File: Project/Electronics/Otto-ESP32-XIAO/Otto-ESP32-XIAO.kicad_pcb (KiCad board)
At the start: 2 copper layers, 60 x 50 mm, 28 parts, among them J1 Conn_01x03, J10 Conn_01x02, J11 Conn_01x04, J12 Conn_01x04, J2 Conn_01x03, J3 Conn_01x03, J4 Conn_01x03, J5 Conn_01x03, J6 Conn_01x03, J7 Conn_01x04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

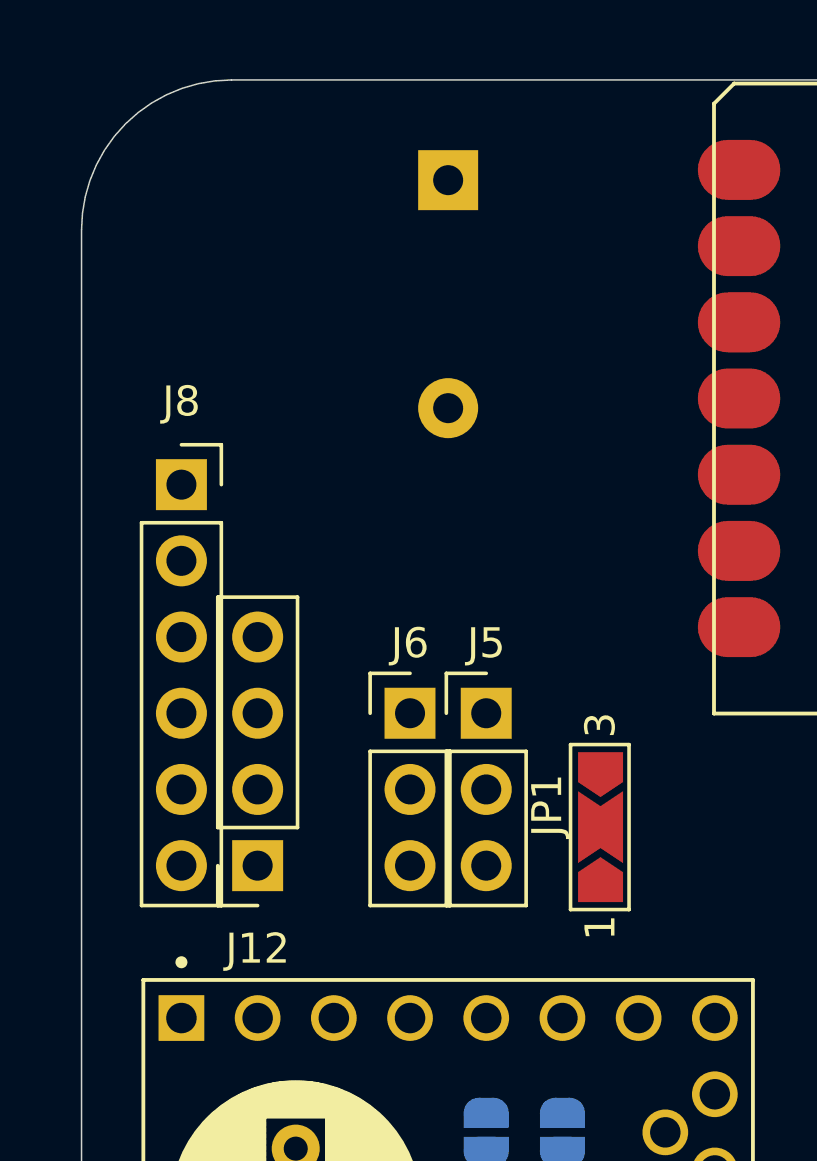
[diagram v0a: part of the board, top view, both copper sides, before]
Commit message: add TMC, oled and 3D models
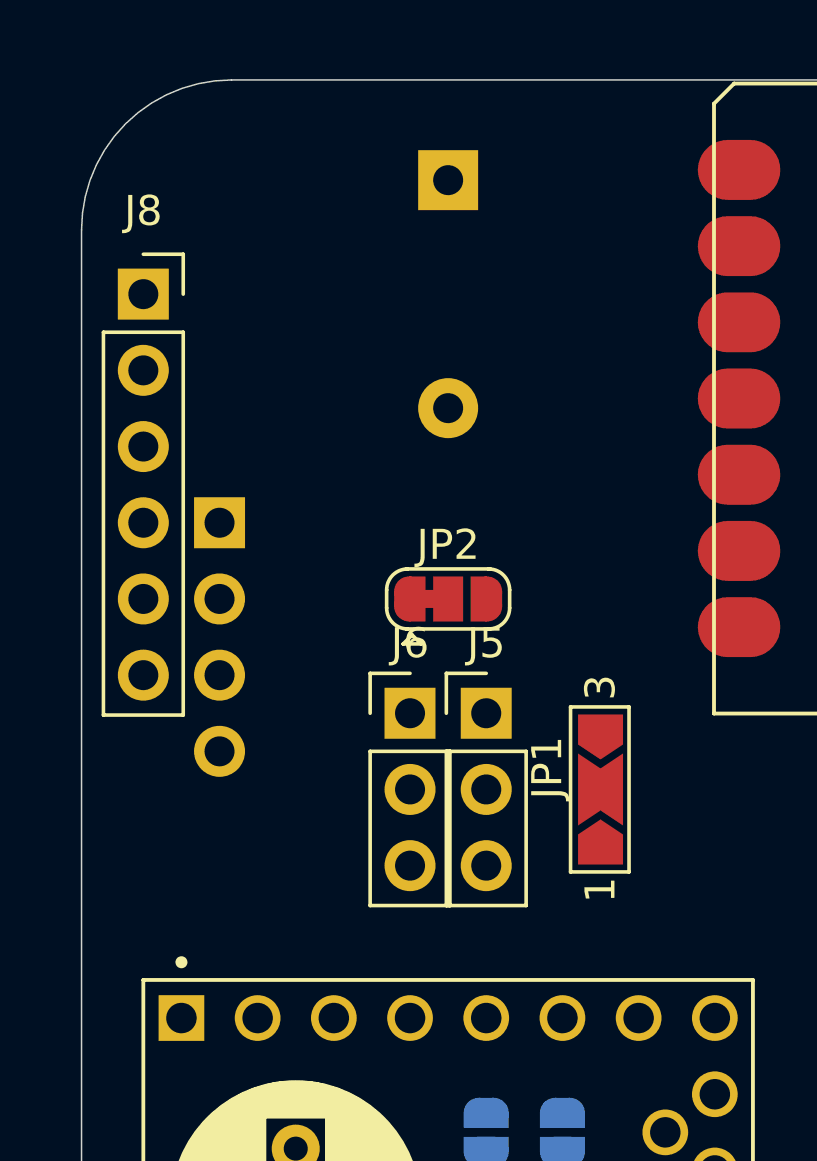
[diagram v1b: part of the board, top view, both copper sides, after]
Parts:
- added JP2: SolderJumper_3_Bridged12, Jumper:SolderJumper-3_P1.3mm_Bridged12_RoundedPad1.0x1.5mm, F.Cu at (112.2, 67.3)
- J12: value Conn_01x04 -> OLED 0,91" - I2C (SKU21796); moved to B.Cu
- moved J12 11.5 mm to (104.6, 64.8)
- moved J8 6.48 mm to (102.1, 57.1)
- moved JP1 1.25 mm to (117.3, 73.7)
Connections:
- J12 pad 2: SCL -> +3.3V
- J12 pad 3: SDA -> SCL
- J12 pad 4: +3.3V -> SDA
- U1 pad 4: Servo-6 -> Net-(JP2-C)
- U3 pad JP1_8: unconnected-(U3-EN-PadJP1_8) -> EN-Driver
- U3 pad JP2_3: Net-(J11-Pin_2) -> Net-(J11-Pin_1)
- U3 pad JP2_4: Net-(J11-Pin_1) -> Net-(J11-Pin_2)
- U4 pad JP1_8: unconnected-(U4-EN-PadJP1_8) -> EN-Driver
- U4 pad JP2_3: Net-(J9-Pin_2) -> Net-(J9-Pin_1)
- U4 pad JP2_4: Net-(J9-Pin_1) -> Net-(J9-Pin_2)

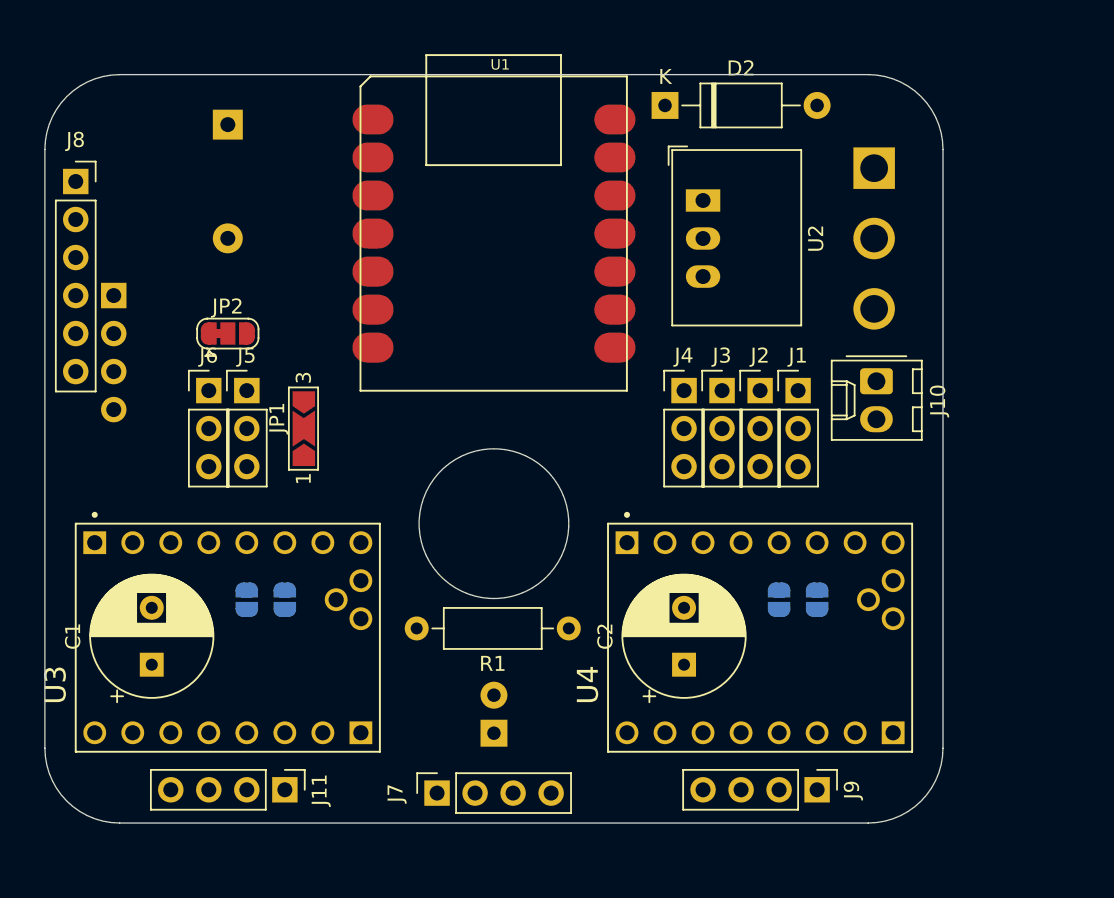
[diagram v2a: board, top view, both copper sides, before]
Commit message: Change US sensor orientation. Add MPU6090
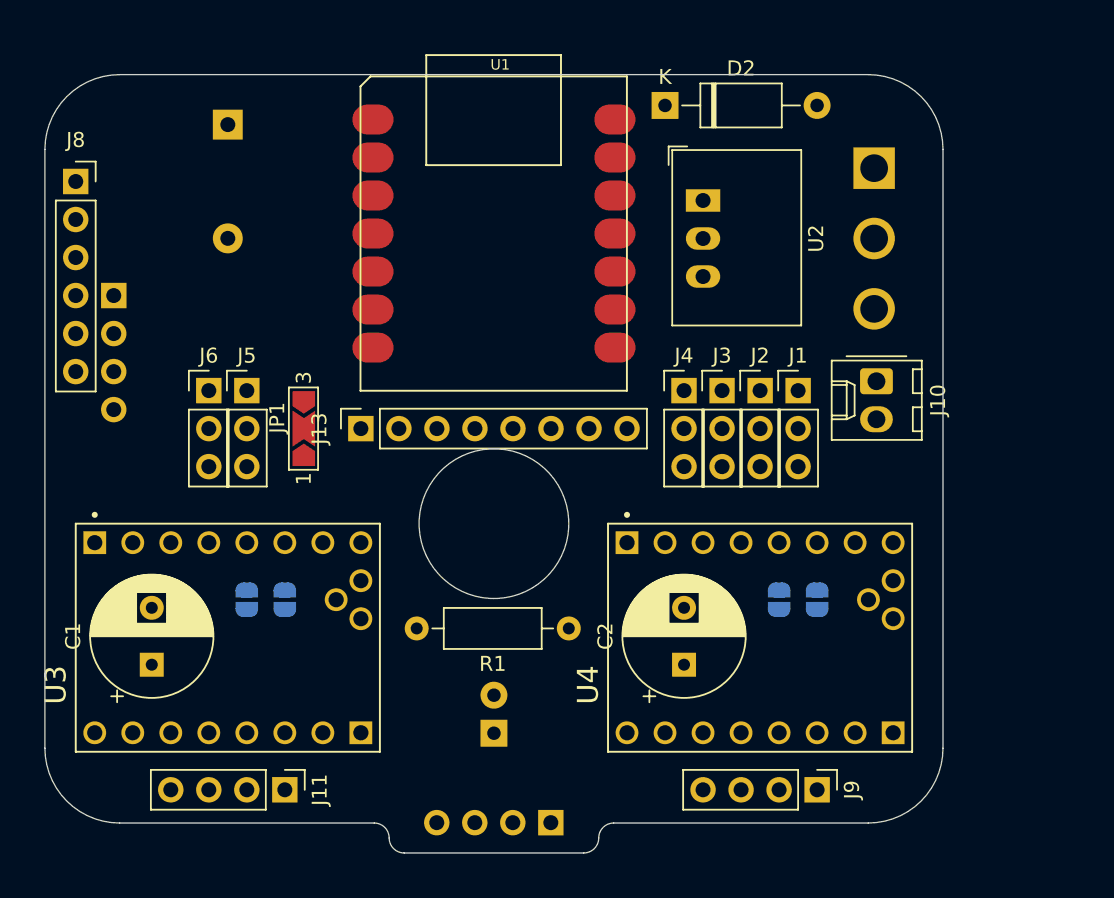
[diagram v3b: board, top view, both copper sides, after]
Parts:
- removed JP2: SolderJumper_3_Bridged12, Jumper:SolderJumper-3_P1.3mm_Bridged12_RoundedPad1.0x1.5mm
- added J13: MPU6050, Connector_PinSocket_2.54mm:PinSocket_1x08_P2.54mm_Vertical, F.Cu at (121.1, 73.7)
- J7: moved to B.Cu
- J8: value Conn_01x06 -> PCA9685
- moved J7 7.85 mm to (133.8, 100.0)
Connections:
- J6 pad 1: Servo-6 -> EN-Driver
- JP3 pad 1: unconnected-(JP3-A-Pad1) -> +3.3V
- JP4 pad 1: unconnected-(JP4-A-Pad1) -> +3.3V
- JP6 pad 1: unconnected-(JP6-A-Pad1) -> +3.3V
- JP7 pad 1: unconnected-(JP7-A-Pad1) -> +3.3V
- U1 pad 4: Net-(JP2-C) -> EN-Driver
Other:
- board size 60 x 50 mm -> 60 x 52 mm

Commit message: routing and documentation
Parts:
- added G***: LOGO, LOGO, F.Cu at (102.1, 71.6)
- added G***: LOGO, LOGO, F.Cu at (150.3, 78.0)
- added G***: LOGO, LOGO, F.Cu at (101.5, 94.0)
- added G***: LOGO, LOGO, F.Cu at (137.1, 94.0)
- added G***: LOGO, LOGO, F.Cu at (155.6, 74.8)
- added G***: LOGO, LOGO, F.Cu at (116.0, 68.3)
- added G***: LOGO, LOGO, F.Cu at (123.6, 75.4)
- added G***: LOGO, LOGO, F.Cu at (133.8, 97.7)
- added G***: LOGO, LOGO, F.Cu at (113.5, 78.0)
- added kibuzzard-66E45A06: G***, kibuzzard-66E45A06, F.Cu at (117.3, 70.3)
- added kibuzzard-66E45A30: G***, kibuzzard-66E45A30, F.Cu at (117.3, 77.0)
- added kibuzzard-66E45AAF: G***, kibuzzard-66E45AAF, F.Cu at (155.5, 68.2)
- added kibuzzard-66E45B15: G***, kibuzzard-66E45B15, F.Cu at (109.1, 73.7)
- added kibuzzard-66E45B15: G***, kibuzzard-66E45B15, F.Cu at (140.9, 73.7)
- added kibuzzard-66E45B34: G***, kibuzzard-66E45B34, F.Cu at (142.6, 69.2)
- added kibuzzard-66E45B47: G***, kibuzzard-66E45B47, F.Cu at (145.2, 69.2)
- added kibuzzard-66E45B4D: G***, kibuzzard-66E45B4D, F.Cu at (147.7, 69.2)
- added kibuzzard-66E45B51: G***, kibuzzard-66E45B51, F.Cu at (150.2, 69.2)
- added kibuzzard-66E45B85: G***, kibuzzard-66E45B85, F.Cu at (113.4, 69.2)
- added kibuzzard-66E45B8A: G***, kibuzzard-66E45B8A, F.Cu at (110.8, 69.2)
- added kibuzzard-66E45BAB: G***, kibuzzard-66E45BAB, F.Cu at (104.8, 57.2)
- added kibuzzard-66E45BBF: G***, kibuzzard-66E45BBF, F.Cu at (105.4, 59.7)
- added kibuzzard-66E45BE1: G***, kibuzzard-66E45BE1, F.Cu at (104.8, 62.2)
- added kibuzzard-66E45BF0: G***, kibuzzard-66E45BF0, F.Cu at (104.8, 64.7)
- added kibuzzard-66E45C62: G***, kibuzzard-66E45C62, F.Cu at (107.3, 63.3)
- added kibuzzard-66E45C9B: G***, kibuzzard-66E45C9B, F.Cu at (109.7, 63.3)
- added kibuzzard-66E45DA3: G***, kibuzzard-66E45DA3, F.Cu at (154.2, 54.2)
- added kibuzzard-66E45E2B: G***, kibuzzard-66E45E2B, F.Cu at (119.5, 79.5)
- added kibuzzard-66E45E2B: G***, kibuzzard-66E45E2B, F.Cu at (155.1, 79.5)
- added kibuzzard-66E45EDE: G***, kibuzzard-66E45EDE, B.Cu at (153.1, 84.5)
- added kibuzzard-66E45EDE: G***, kibuzzard-66E45EDE, B.Cu at (117.5, 84.5)
- added kibuzzard-66E45EFB: G***, kibuzzard-66E45EFB, B.Cu at (147.6, 84.5)
- added kibuzzard-66E45EFB: G***, kibuzzard-66E45EFB, B.Cu at (112.0, 84.5)
- added kibuzzard-66E45FF5: G***, kibuzzard-66E45FF5, F.Cu at (155.4, 97.8)
- added kibuzzard-66E45FFF: G***, kibuzzard-66E45FFF, F.Cu at (104.7, 97.7)
- added kibuzzard-66E460A4: G***, kibuzzard-66E460A4, F.Cu at (109.9, 67.9)
- added kibuzzard-66E460BA: G***, kibuzzard-66E460BA, F.Cu at (103.9, 68.7)
- added kibuzzard-66E460D9: G***, kibuzzard-66E460D9, F.Cu at (136.0, 75.5)
- added kibuzzard-66E46157: G***, kibuzzard-66E46157, F.Cu at (127.6, 98.1)
- added kibuzzard-66E461B7: G***, kibuzzard-66E461B7, B.Cu at (128.2, 56.2)
- added kibuzzard-66E462B0: G***, kibuzzard-66E462B0, B.Cu at (131.5, 55.6)
- moved J12 11.5 mm to (116.0, 66.0), turned to 90 degrees
- moved SW1 10.2 mm to (145.2, 61.0)
- moved U2 7.95 mm to (151.9, 58.4)
- moved D2 1.49 mm to (142.9, 52.1)
- moved JP3 0.62 mm to (116.0, 84.5)
- moved JP4 0.62 mm to (113.5, 84.5)
- moved JP6 0.62 mm to (151.6, 84.5)
- moved JP7 0.62 mm to (149.1, 84.5)
- moved BZ1 0.37 mm to (112.5, 53.1)
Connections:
- C1 pad 1: +5VP -> +BATT
- C2 pad 1: +5VP -> +BATT
- U3 pad JP1_1: Servo-4 -> Servo-3
- U3 pad JP1_2: Servo-3 -> Servo-4
- U4 pad JP1_1: Servo-1 -> Servo-2
- U4 pad JP1_2: Servo-2 -> Servo-1
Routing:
- net +3.3V: track 0.00 -> 156.0 mm, vias 0 -> 1
- net +5V: track 0.00 -> 126.6 mm
- net +BATT: track 0.00 -> 120.0 mm
- net EN-Driver: track 0.00 -> 94.7 mm, vias 0 -> 2
- net Echo: track 0.00 -> 59.1 mm, vias 0 -> 1
- net Trig: track 0.00 -> 58.3 mm, vias 0 -> 1
- net Servo-3: track 0.00 -> 55.8 mm, vias 0 -> 1
- net Servo-4: track 0.00 -> 49.1 mm, vias 0 -> 1
- net SDA: track 0.00 -> 37.6 mm
- net Servo-1: track 0.00 -> 36.9 mm
- net SCL: track 0.00 -> 35.4 mm
- net Servo-2: track 0.00 -> 31.7 mm
- net Net-(J10-Pin_1): track 0.00 -> 14.3 mm
- net Servo-5: track 0.00 -> 10.5 mm, vias 0 -> 1
- net Buzzer: track 0.00 -> 9.48 mm
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- added copper zone on B.Cu, net GND
- added copper zone on F.Cu, net GND

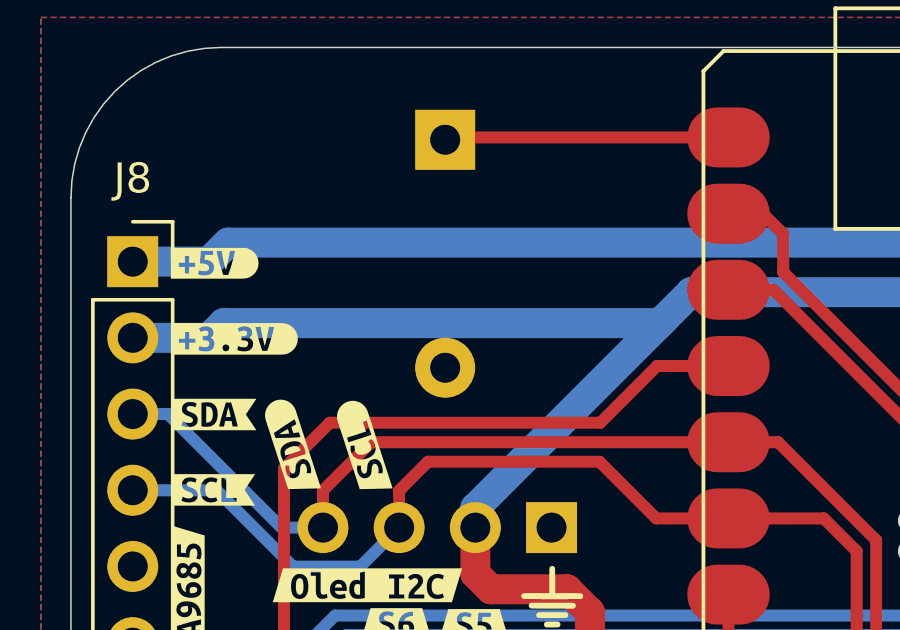
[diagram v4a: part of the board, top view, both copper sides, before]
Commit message: correct short circuit between gnd and 3.3V
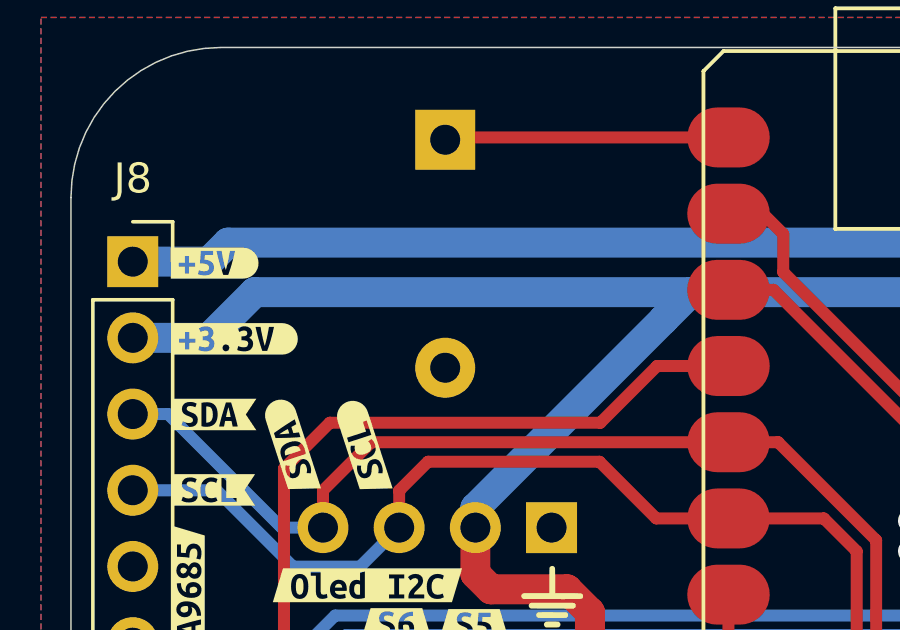
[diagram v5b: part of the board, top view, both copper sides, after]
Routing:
- net +3.3V: track 156.0 -> 157.3 mm
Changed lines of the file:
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@@
+	)
+	(segment
+		(start 104.6 59.68)
+		(end 106.124 58.156)
+		(width 1)
+		(layer "B.Cu")
+		(net 11)
 	)
 	(segment
 		(start 140.414 92.192)
 		(end 137.874 89.652)
+		(width 1)
+		(layer "B.Cu")
+		(net 11)
+	)
+	(segment
+		(start 106.124 58.156)
+		(end 120.669 58.156)
 		(width 1)
 		(layer "B.Cu")
@@
 		(start 120.669 58.156)
 		(end 119.7465 59.0785)
-		(width 1)
-		(layer "B.Cu")
-		(net 11)
-	)
-	(segment
-		(start 105.09 59.19)
-		(end 119.635 59.19)
 		(width 1)
 		(layer "B.Cu")
@@
 	)
 	(segment
-		(start 119.635 59.19)
-		(end 119.7465 59.0785)
+		(start 102.06 59.68)
+		(end 104.6 59.68)
 		(width 1)
 		(layer "B.Cu")
@@
 	)
 	(segment
-		(start 102.06 59.68)
-		(end 104.6 59.68)
-		(width 1)
-		(layer "B.Cu")
-		(net 11)
-	)
-	(segment
 		(start 150.32 90.922)
 		(end 149.05 92.192)
@@
 		(width 1)
 		(layer "B.Cu")
-		(net 11)
-	)
-	(segment
-		(start 104.6 59.68)
-		(end 105.09 59.19)
-		(width 1)
-		(layer "B.Cu")
